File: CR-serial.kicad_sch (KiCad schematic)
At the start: 88 parts, among them J1 USB_B, J2 GPIO, J3 UART0, J4 UART1, J5 UART2, J6 UART3_HV, J7 RS232_0, J8 RS232_1, U1 CP2108-xxx-xM, U10 TVS4201MR6, U11 TVS4201MR6, U12 TVS4201MR6, U13 TVS4201MR6, U14 TVS4201MR6, U15 TVS4201MR6, U2 MAX232, U3 ECMF02-4CMX8, U4 TVS4201MR6, U5 TVS4201MR6, U6 TVS4201MR6, U7 TVS4201MR6, U8 TVS4201MR6, U9 TVS4201MR6

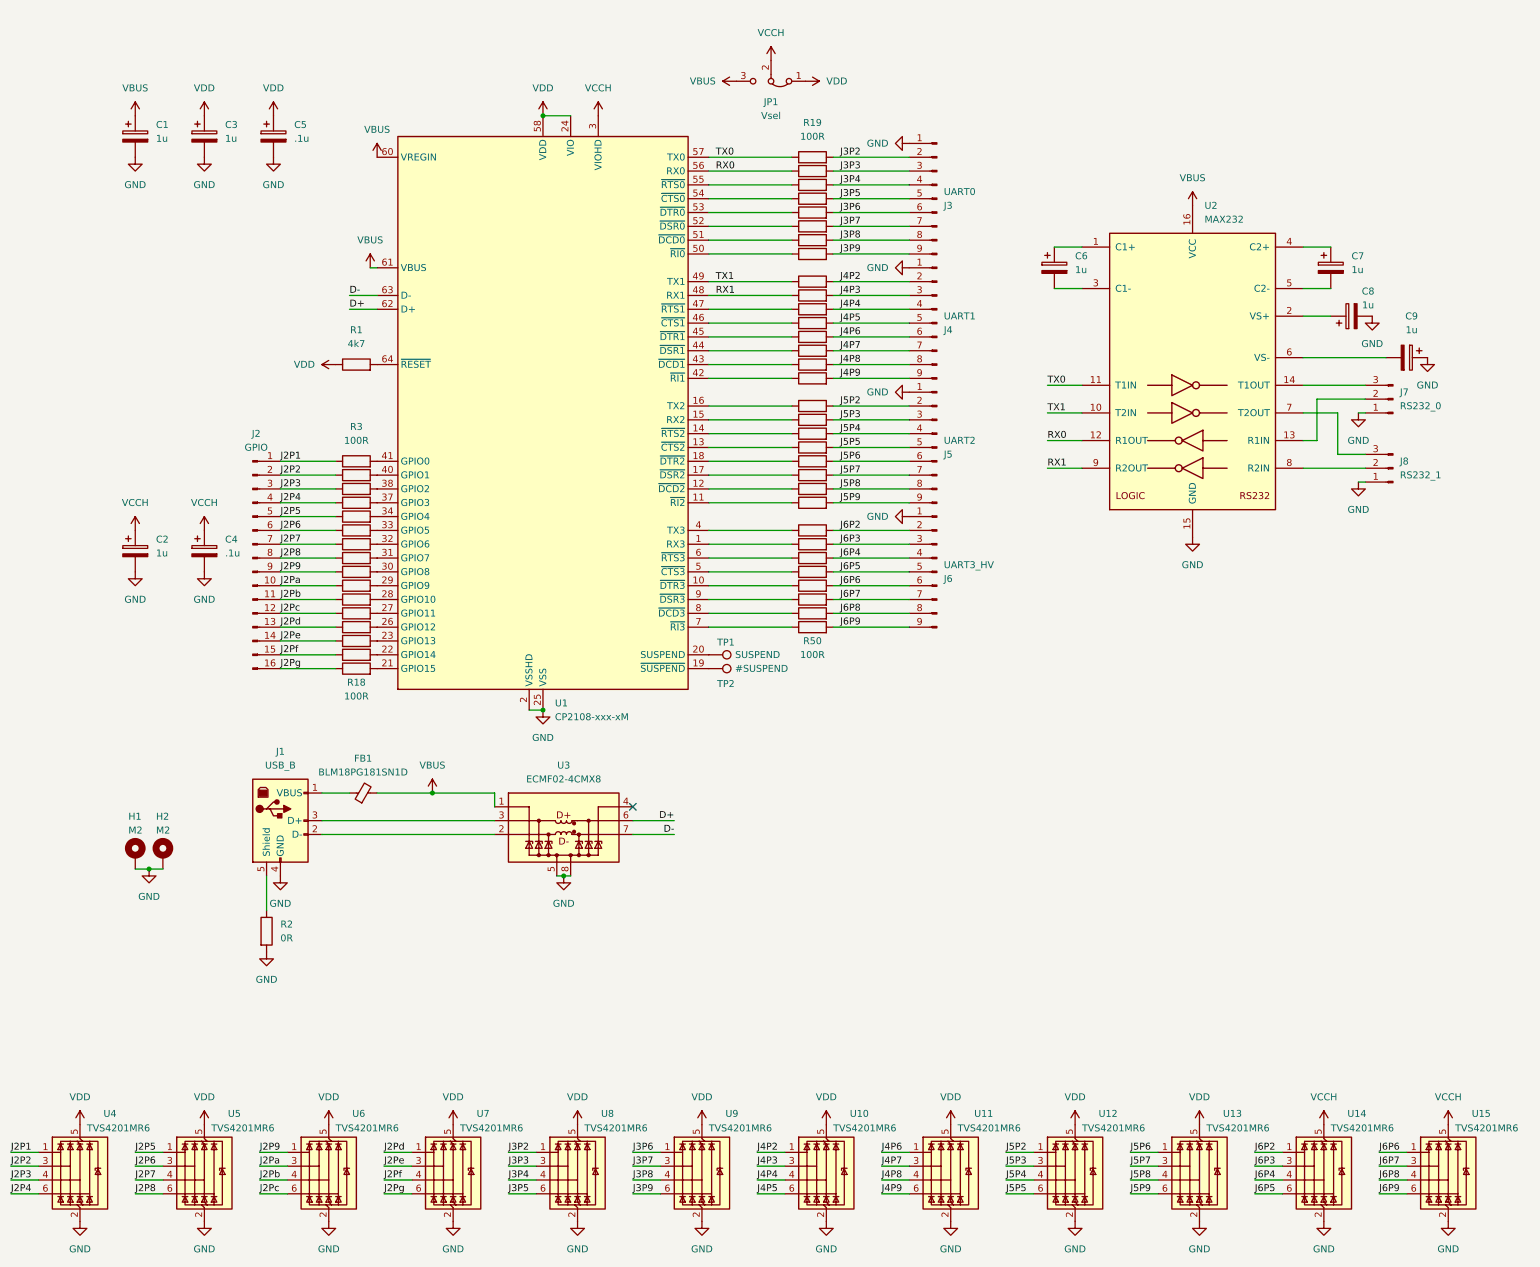
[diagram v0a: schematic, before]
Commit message: Refactor: split out RS-232 driver and misc components
(e.g. bus capacitors, mounting holes)
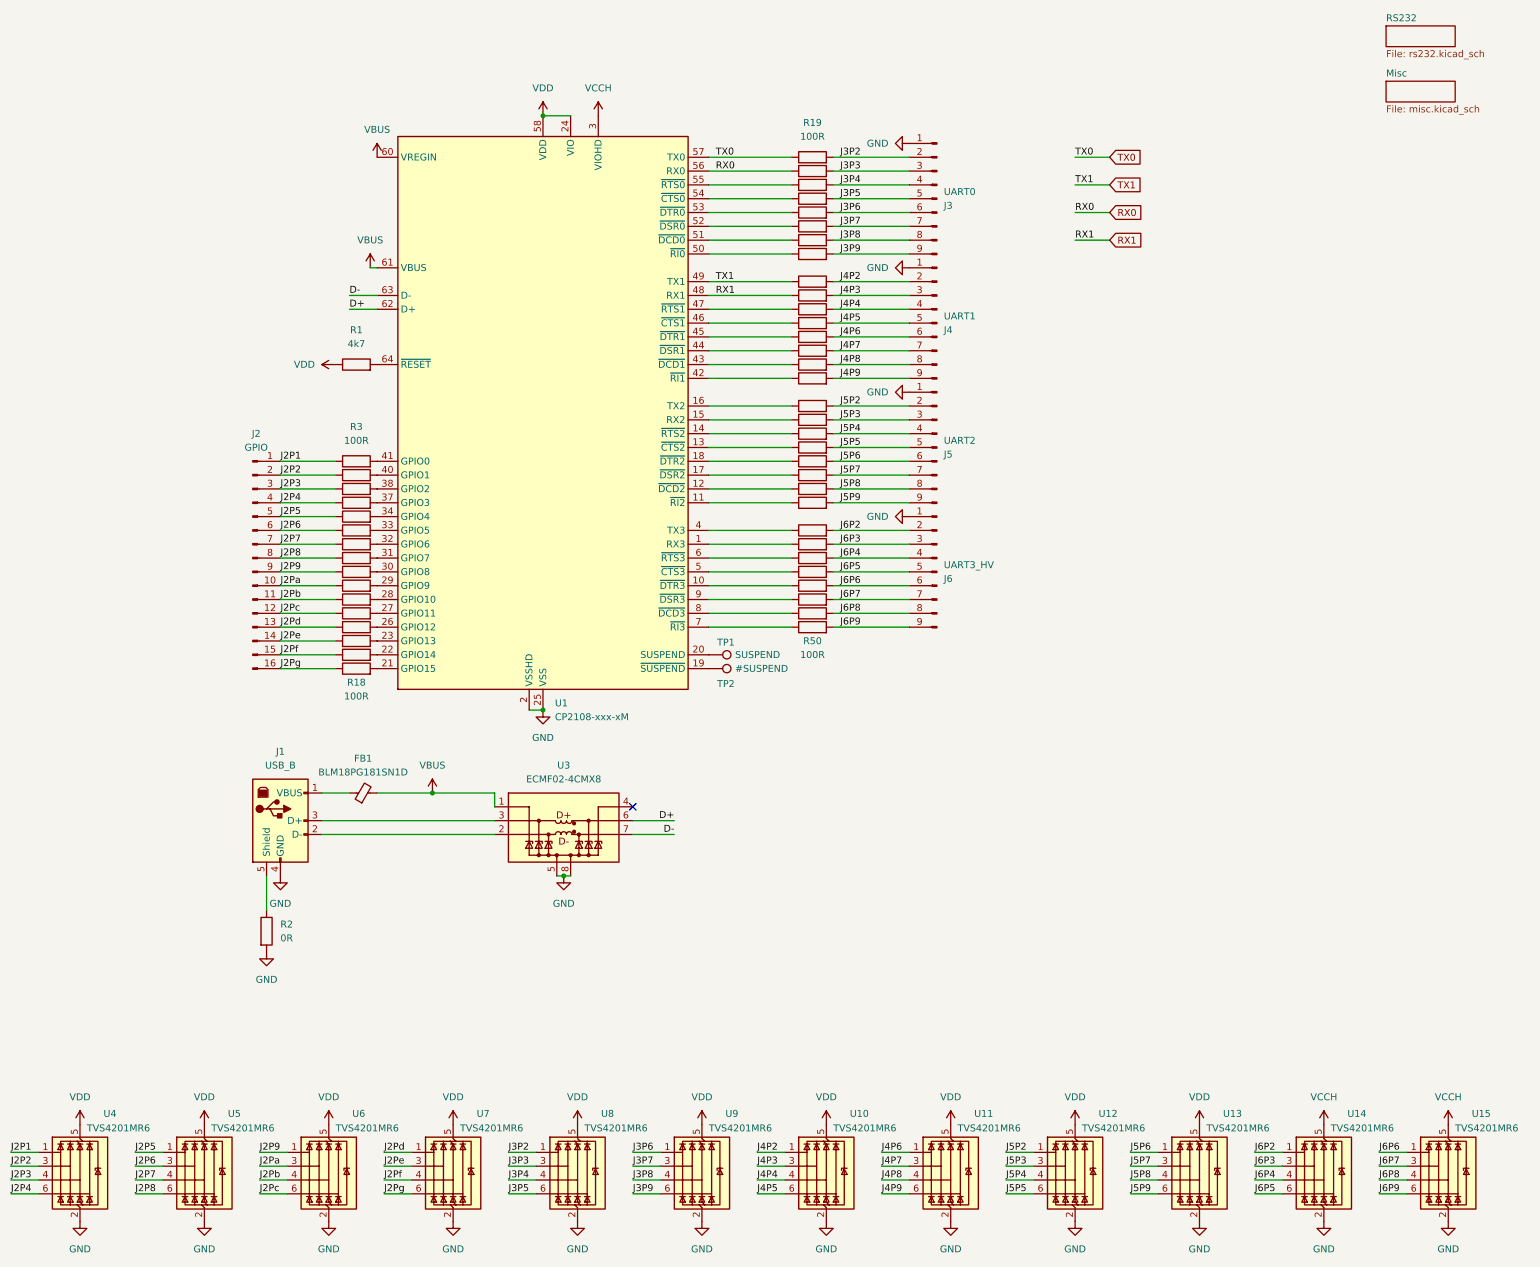
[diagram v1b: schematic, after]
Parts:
- removed C1, C2, C3, C6, C7, C8, C9: 1u, Capacitor_SMD:C_0603_1608Metric, symbol Device:C_Polarized
- removed C4, C5: .1u, Capacitor_SMD:C_0603_1608Metric, symbol Device:C_Polarized
- removed H1, H2: M2, MountingHole:MountingHole_2.2mm_M2_Pad_TopBottom, symbol Mechanical:MountingHole_Pad
- removed J7: RS232_0, Connector_Phoenix_MC:PhoenixContact_MCV_1,5_3-G-3.81_1x03_P3.81mm_Vertical, symbol Connector:Conn_01x03_Pin
- removed J8: RS232_1, Connector_Phoenix_MC:PhoenixContact_MCV_1,5_3-G-3.81_1x03_P3.81mm_Vertical, symbol Connector:Conn_01x03_Pin
- removed JP1: Vsel, Jumper:SolderJumper-3_P1.3mm_Bridged12_RoundedPad1.0x1.5mm_NumberLabels, symbol Jumper:Jumper_3_Bridged12
- removed U2: MAX232, Package_SO:SOIC-16_3.9x9.9mm_P1.27mm, symbol Interface_UART:MAX232
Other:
- added sheet Misc (misc.kicad_sch)
- added sheet RS232 (rs232.kicad_sch)

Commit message: Export common fields to all sheets
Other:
- company: Prolan -> TXnology
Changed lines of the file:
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@@
 	(title_block
 		(title "USB-to-quad UART")
-		(date "2024-07-31")
+		(date "2024-08-30")
 		(rev "rev. 2")
-		(company "Prolan")
-		(comment 1 "USB")
+		(company "TXnology")
+		(comment 1 "Engineer: Bence Csókás")
 	)
 	(junction

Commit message: WIP: Refactor: split out UART headers to a new page
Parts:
- removed J2: GPIO, Connector_PinHeader_2.54mm:PinHeader_2x08_P2.54mm_Vertical, symbol Connector:Conn_01x16_Pin
- removed J3: UART0, Connector_PinHeader_2.54mm:PinHeader_1x09_P2.54mm_Vertical, symbol Connector:Conn_01x09_Pin
- removed J4: UART1, Connector_PinHeader_2.54mm:PinHeader_1x09_P2.54mm_Vertical, symbol Connector:Conn_01x09_Pin
- removed J5: UART2, Connector_PinHeader_2.54mm:PinHeader_1x09_P2.54mm_Vertical, symbol Connector:Conn_01x09_Pin
- removed J6: UART3_HV, Connector_PinHeader_2.54mm:PinHeader_1x09_P2.54mm_Vertical, symbol Connector:Conn_01x09_Pin
- removed R10, R11, R12, R13, R14, R15, R16, R17, R18, R19, R20, R21, R22, R23, R24, R25, R26, R27, R28, R29, R3, R30, R31, R32, R33, R34, R35, R36, R37, R38, R39, R4, R40, R41, R42, R43, R44, R45, R46, R47, R48, R49, R5, R50, R6, R7, R8, R9: 100R, Resistor_SMD:R_0603_1608Metric, symbol Device:R
- removed U10, U11, U12, U13, U14, U15, U4, U5, U6, U7, U8, U9: TVS4201MR6, Package_SO:TSOP-6_1.65x3.05mm_P0.95mm, symbol QCP_parts:TVS4201MR6
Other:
- added sheet UART (uart.kicad_sch)
